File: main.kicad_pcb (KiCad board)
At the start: 2 copper layers, 268.1 x 124.6 mm, 115 parts, among them SW1 Kailh-Choc, SW10 Kailh-Choc, SW11 Kailh-Choc, SW12 Kailh-Choc, SW13 Kailh-Choc, SW14 Kailh-Choc, SW15 Kailh-Choc, SW16 Kailh-Choc, SW17 Kailh-Choc, SW18 Kailh-Choc, SW19 Kailh-Choc, SW2 Kailh-Choc, SW20 Kailh-Choc, SW21 Kailh-Choc, SW22 Kailh-Choc, SW23 Kailh-Choc, SW24 Kailh-Choc, SW25 Kailh-Choc, SW26 Kailh-Choc, SW27 Kailh-Choc, SW28 Kailh-Choc, SW29 Kailh-Choc, SW3 Kailh-Choc, SW30 Kailh-Choc, SW31 Kailh-Choc, SW32 Kailh-Choc, SW33 Kailh-Choc, SW34 Kailh-Choc, SW35 Kailh-Choc, SW36 Kailh-Choc, SW37 Kailh-Choc, SW38 Kailh-Choc, SW39 Kailh-Choc, SW4 Kailh-Choc, SW40 Kailh-Choc, SW5 Kailh-Choc, SW6 Kailh-Choc, SW7 Kailh-Choc, SW8 Kailh-Choc, SW9 Kailh-Choc, U1 nice_nano, U2 nice_nano

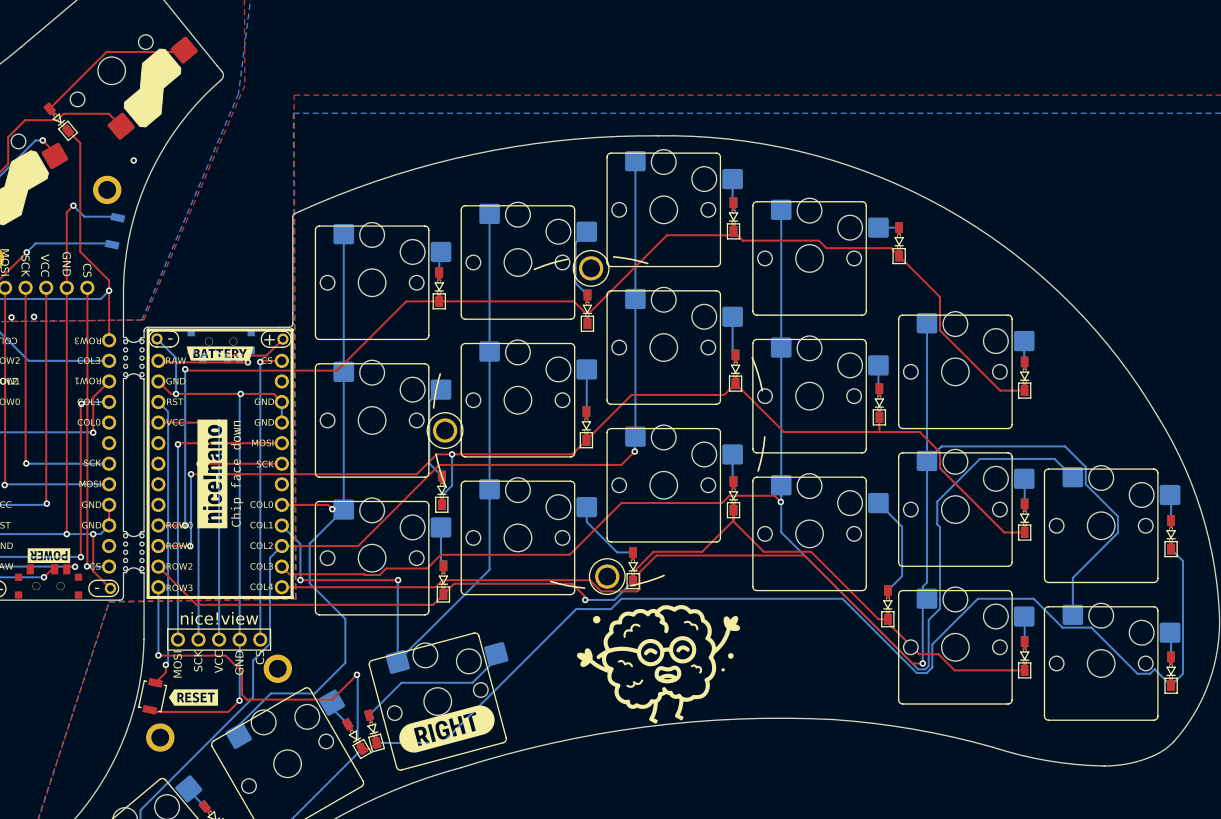
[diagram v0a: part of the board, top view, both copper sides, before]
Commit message: Fixed issue with hole cutting trace. updated version
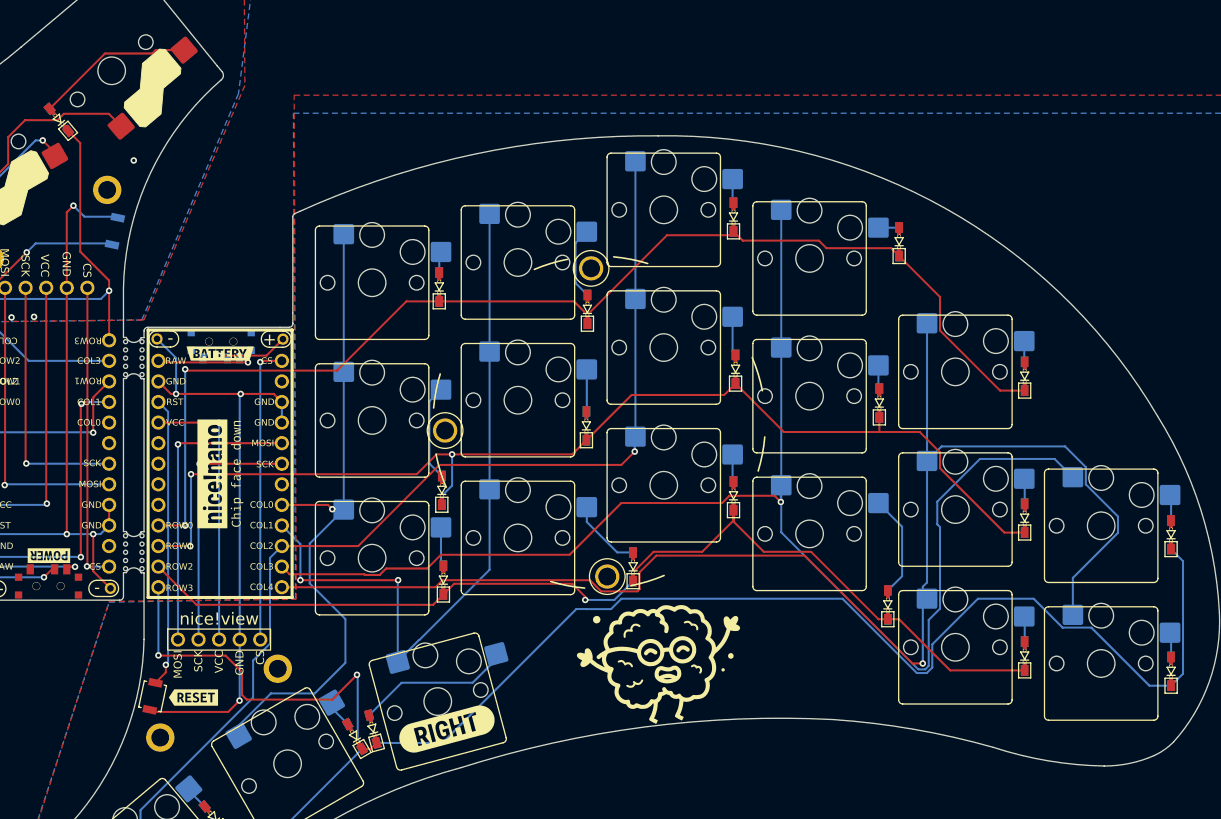
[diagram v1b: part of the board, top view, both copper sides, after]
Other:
- board text added: "Brain 0.3.0"
- board text removed: "Brain 0.2.0"

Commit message: Removed alot of small unconnected traces
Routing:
- net Net-(D6-A): track 3.29 -> 2.73 mm
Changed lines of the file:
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@@
   (segment (start 122.626239 165.193144) (end 122.626239 167.98564) (width 0.25) (layer "F.Cu") (net 2))
   (segment (start 122.626239 167.98564) (end 122.466237 168.145642) (width 0.25) (layer "F.Cu") (net 2))
-  (segment (start 140.46624 179.071143) (end 140.533239 179.004144) (width 0.25) (layer "F.Cu") (net 3))
   (segment (start 140.533239 179.004144) (end 140.533239 182.078642) (width 0.25) (layer "F.Cu") (net 3))
   (segment (start 140.533239 182.078642) (end 140.46624 182.145641) (width 0.25) (layer "F.Cu") (net 3))
@@
   (segment (start 167.822423 158.055144) (end 172.129202 158.055144) (width 0.25) (layer "B.Cu") (net 7))
   (segment (start 190.531639 149.924144) (end 191.332495 149.123288) (width 0.25) (layer "B.Cu") (net 7))
-  (segment (start 122.428 148.449987) (end 122.625278 148.252709) (width 0.25) (layer "F.Cu") (net 8))
-  (segment (start 122.625278 150.986606) (end 122.466239 151.145645) (width 0.25) (layer "F.Cu") (net 8))
   (segment (start 122.625278 148.252709) (end 122.625278 150.986606) (width 0.25) (layer "F.Cu") (net 8))
-  (segment (start 122.466239 151.145645) (end 122.428 151.107406) (width 0.25) (layer "F.Cu") (net 8))
   (segment (start 140.533239 165.078649) (end 140.533239 161.224144) (width 0.25) (layer "F.Cu") (net 9))
   (segment (start 140.466242 165.145646) (end 140.533239 165.078649) (width 0.25) (layer "F.Cu") (net 9))
@@
   (segment (start 176.601239 143.825144) (end 176.601239 147.510143) (width 0.25) (layer "F.Cu") (net 17))
   (segment (start 176.601239 147.510143) (end 176.465239 147.646143) (width 0.25) (layer "F.Cu") (net 17))
-  (segment (start 176.465239 143.961144) (end 176.601239 143.825144) (width 0.25) (layer "F.Cu") (net 17))
   (segment (start 194.466244 145.146145) (end 192.854239 143.53414) (width 0.25) (layer "F.Cu") (net 18))
   (segment (start 192.854239 143.53414) (end 192.854239 132.906144) (width 0.25) (layer "F.Cu") (net 18))
   (segment (start 117.713679 132.420642) (end 117.888679 132.245642) (width 0.25) (layer "F.Cu") (net 19))
   (segment (start 208.787888 126.822318) (end 208.787888 113.409675) (width 0.25) (layer "F.Cu") (net 19))
-  (segment (start 104.861423 142.410196) (end 104.648 142.196773) (width 0.25) (layer "F.Cu") (net 19))
   (segment (start 212.351269 131.648318) (end 212.351269 137.762477) (width 0.25) (layer "F.Cu") (net 19))
   (segment (start 110.909366 130.935463) (end 110.909366 132.420642) (width 0.25) (layer "F.Cu") (net 19))
@@
   (segment (start 195.905239 120.460144) (end 203.271239 113.094144) (width 0.25) (layer "B.Cu") (net 24))
   (segment (start 253.107895 129.405566) (end 253.107895 127.072291) (width 0.25) (layer "B.Cu") (net 25))
-  (segment (start 253.318649 129.194812) (end 253.107895 129.405566) (width 0.25) (layer "B.Cu") (net 25))
   (segment (start 253.107895 127.072291) (end 253.318649 126.861537) (width 0.25) (layer "B.Cu") (net 25))
   (segment (start 269.928399 125.752789) (end 271.319648 124.36154) (width 0.25) (layer "B.Cu") (net 26))
@@
   (segment (start 222.187077 193.349004) (end 222.187077 193.138039) (width 0.25) (layer "B.Cu") (net 51))
   (segment (start 224.144382 195.306309) (end 222.187077 193.349004) (width 0.25) (layer "B.Cu") (net 51))
-  (segment (start 343.318651 159.868554) (end 343.444869 159.994772) (width 0.25) (layer "B.Cu") (net 52))
   (segment (start 343.444869 159.994772) (end 343.444869 156.988252) (width 0.25) (layer "B.Cu") (net 52))
   (segment (start 343.444869 156.988252) (end 343.318651 156.862034) (width 0.25) (layer "B.Cu") (net 52))
@@
       05c7472c-d677-459d-bc53-e528654d7515
       05f92425-e314-4ebc-ba7a-b6580e6bd212
-      0616cef8-6ea9-4f34-a4ef-59ff4db7ae94
       062ca4a6-a17d-4258-8974-3f1d8baa0ddd
       06dfb762-14ff-4833-b5db-eff60036fffa
@@
       d8359f09-cf00-493b-bbe0-15e254b03de1
       d85d05ba-833c-44fa-b64f-70555303b5df
-      d8a7750d-3058-40de-9765-ed179e712a92
       d8f4f757-e102-4924-ae05-381d2ff4dd1a
       d920113d-1998-4392-ad0c-e4b1edf423a9
@@
       022398b7-104e-4f56-a0a4-19b5f92c42ae
       0311cb8d-56bc-4ba9-aaa5-5fa4ec19c326
-      039df08e-7422-4323-ab2a-734351cf2492
       040f8366-6962-4e2b-91d5-b02a643bc030
       05a8e57e-04e7-42e1-aec7-2a5f2830fa1f
@@
       0ba87ad2-bf19-415d-946a-3a3e849ea6e4
       0bd16bc1-3648-4b4a-8600-80e6e2ae863e
-      0bf490b6-c584-401b-a0a2-65d4547bbab2
       0c3dcf15-5e43-4bec-a927-2e33ca75a7d1
       0c4cda46-db31-4a02-8ed1-3f93820ee232
@@
       5d5b1284-3ca9-4ac3-b409-28537e6a743f
       5d614093-44aa-4bcd-bf75-f5385da398c0
-      5e1d3601-2734-4961-b5df-2b2c4c0a3bde
       5e538131-c3ed-4af8-b647-59a1bdb8a7bd
       5e8f251b-27ec-4938-b743-44f9067e0266
@@
       a0d2a1d8-2382-4c6f-ac80-c554369e1537
       a1bb8b0f-d6ca-4def-ba2a-461bdaa71554
-      a2b35acf-01d5-41ab-9561-33f92d8ec211
       a2ba3940-c074-426a-8fa5-c32dc951fcef
       a43e907f-0a2f-4181-970d-0aea20d6ea47
@@
       a4a8961a-8a2d-43a5-801a-3be8cd892312
       a53f0838-431c-4bf3-af56-37ba9f332b74
-      a5de53e1-92c0-40da-8cf7-c8699f164bc6
       a6a5caee-7104-46c4-a4f2-11f9c024f1ad
       a6fa385d-1873-4b0d-ba25-393bbcd52ecd
@@
       cdd99773-1c6e-4b0e-86b5-97c48a517ebf
       ce64c5da-4775-4181-89de-111fc65135e6
-      ce86a94d-8388-46a9-80db-7ed03bdc7546
       cef9bd80-357a-4f8e-9029-25993c90bc0e
       cfa2cd23-0361-417c-91ba-7ff5b10c5d45

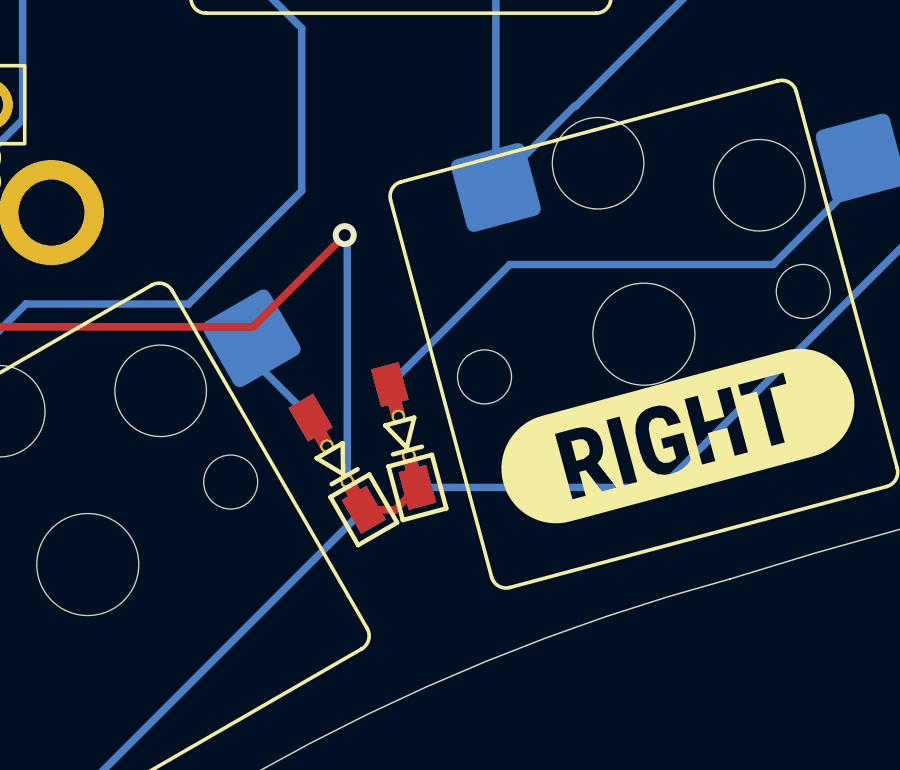
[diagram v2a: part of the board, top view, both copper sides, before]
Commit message: Updated version text to 1.0.0
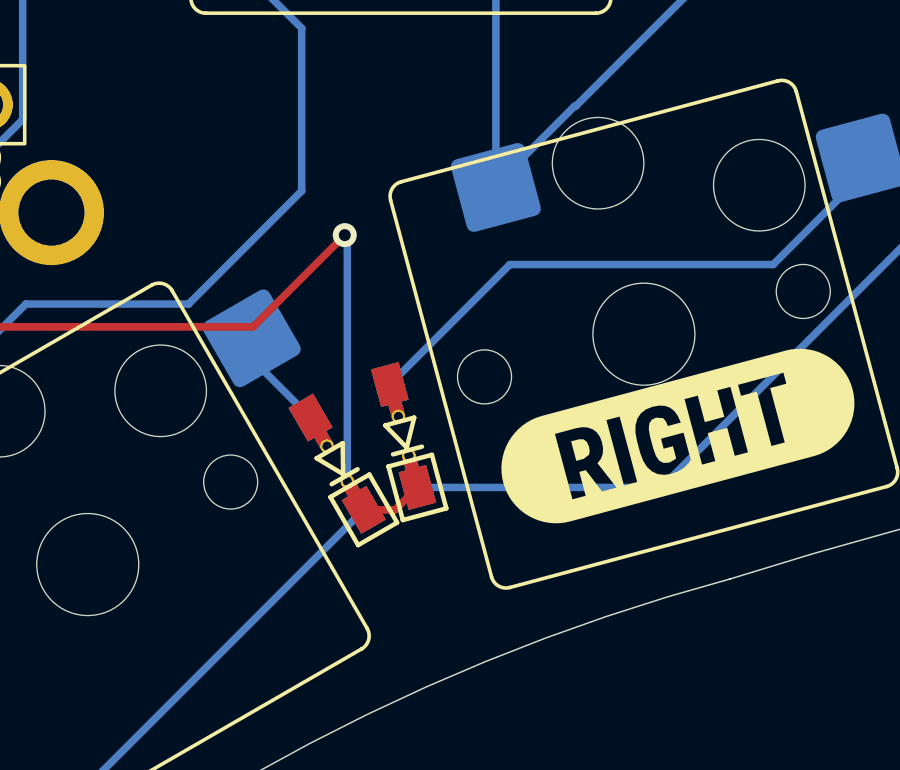
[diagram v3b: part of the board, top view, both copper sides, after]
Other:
- board text added: "Brain 1.0.0"
- board text removed: "Brain 0.3.0"
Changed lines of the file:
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@@
     (fp_line (start 7 6.5) (end 7 -6.5)
       (stroke (width 0.12) (type solid)) (layer "F.SilkS"))
-    (fp_arc (start -7 -6.5) (mid -6.853553 -6.853553) (end -6.5 -7)
+    (fp_arc (start -7 -6.5) (mid -6.853554 -6.853553) (end -6.5 -7)
       (stroke (width 0.12) (type solid)) (layer "F.SilkS"))
-    (fp_arc (start -6.5 7) (mid -6.853553 6.853553) (end -7 6.5)
+    (fp_arc (start -6.5 7) (mid -6.853553 6.853554) (end -7 6.5)
       (stroke (width 0.12) (type solid)) (layer "F.SilkS"))
     (fp_arc (start 6.5 -7) (mid 6.853553 -6.853553) (end 7 -6.5)
@@
     (fp_line (start 7 -6.5) (end 7 6.5)
       (stroke (width 0.12) (type solid)) (layer "B.SilkS"))
-    (fp_arc (start -7 -6.5) (mid -6.853553 -6.853553) (end -6.5 -7)
+    (fp_arc (start -7 -6.5) (mid -6.853554 -6.853553) (end -6.5 -7)
       (stroke (width 0.12) (type solid)) (layer "B.SilkS"))
-    (fp_arc (start -6.5 7) (mid -6.853553 6.853553) (end -7 6.5)
+    (fp_arc (start -6.5 7) (mid -6.853553 6.853554) (end -7 6.5)
       (stroke (width 0.12) (type solid)) (layer "B.SilkS"))
     (fp_arc (start 6.5 -7) (mid 6.853553 -6.853553) (end 7 -6.5)
@@
     (effects (font (size 1 1) (thickness 0.15)) (justify right mirror))
   )
-  (gr_text "Brain 0.3.0" (at 302.514 174.752) (layer "B.SilkS")
+  (gr_text "Brain 1.0.0" (at 302.514 174.752) (layer "B.SilkS")
     (effects (font (size 1 1) (thickness 0.15)) (justify left bottom mirror))
   )
